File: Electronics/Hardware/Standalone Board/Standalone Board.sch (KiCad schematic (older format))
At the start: 4 parts

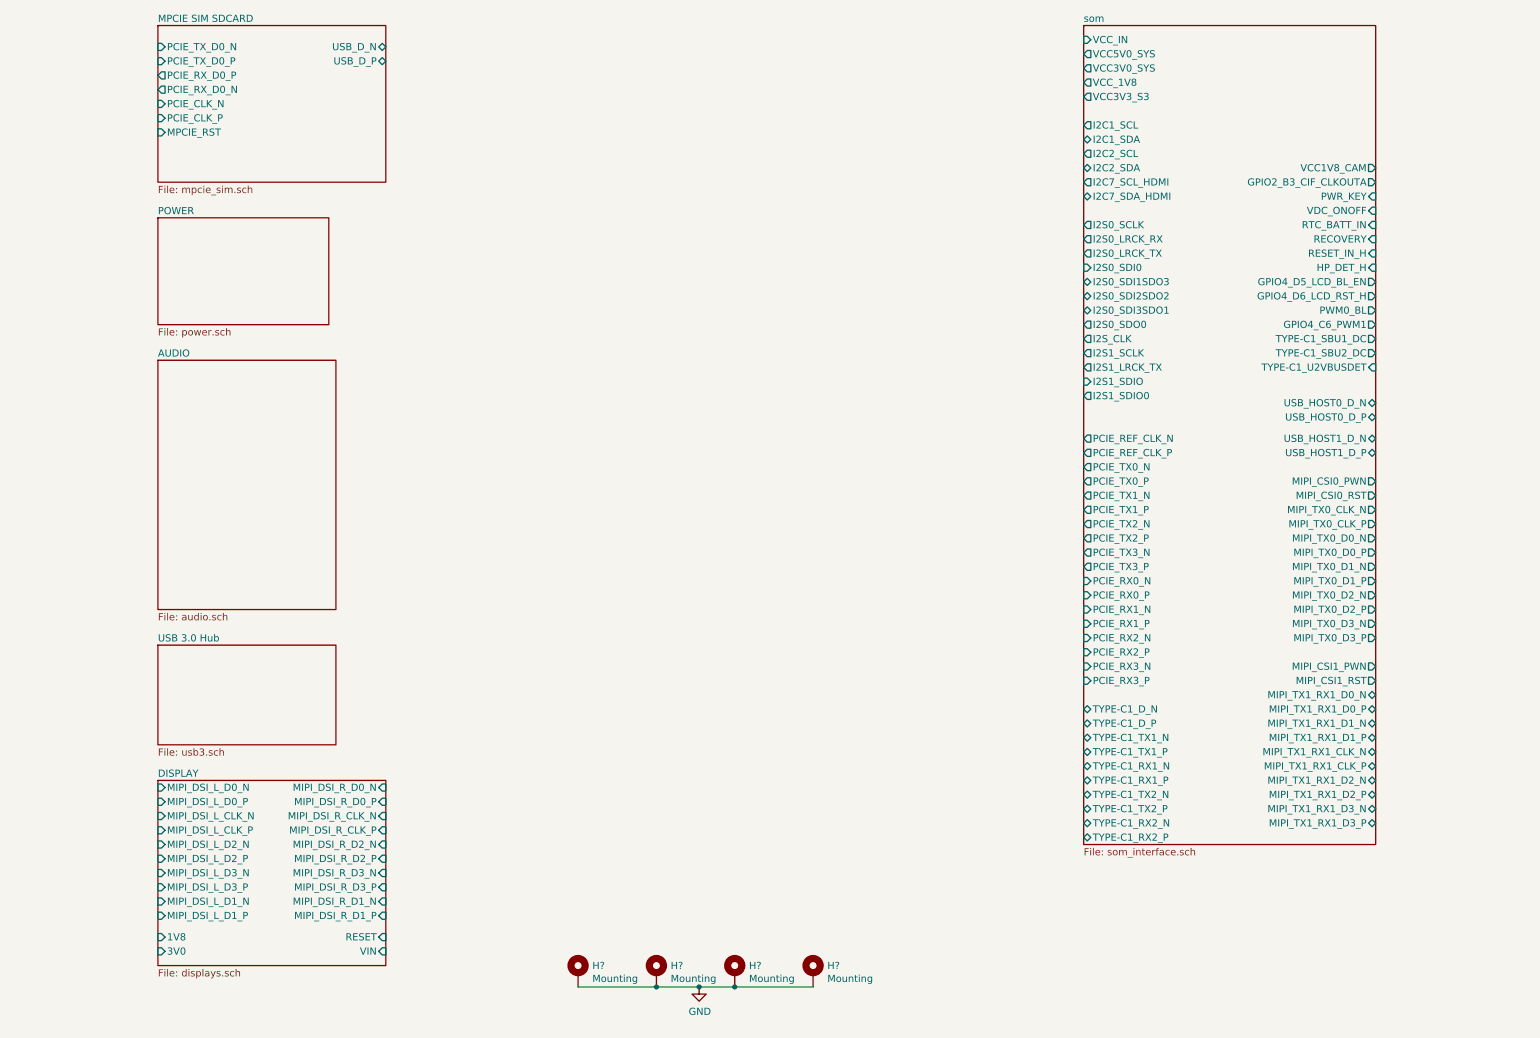
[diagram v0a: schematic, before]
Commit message: Add debug uart, gps uart, fan control and sdcard
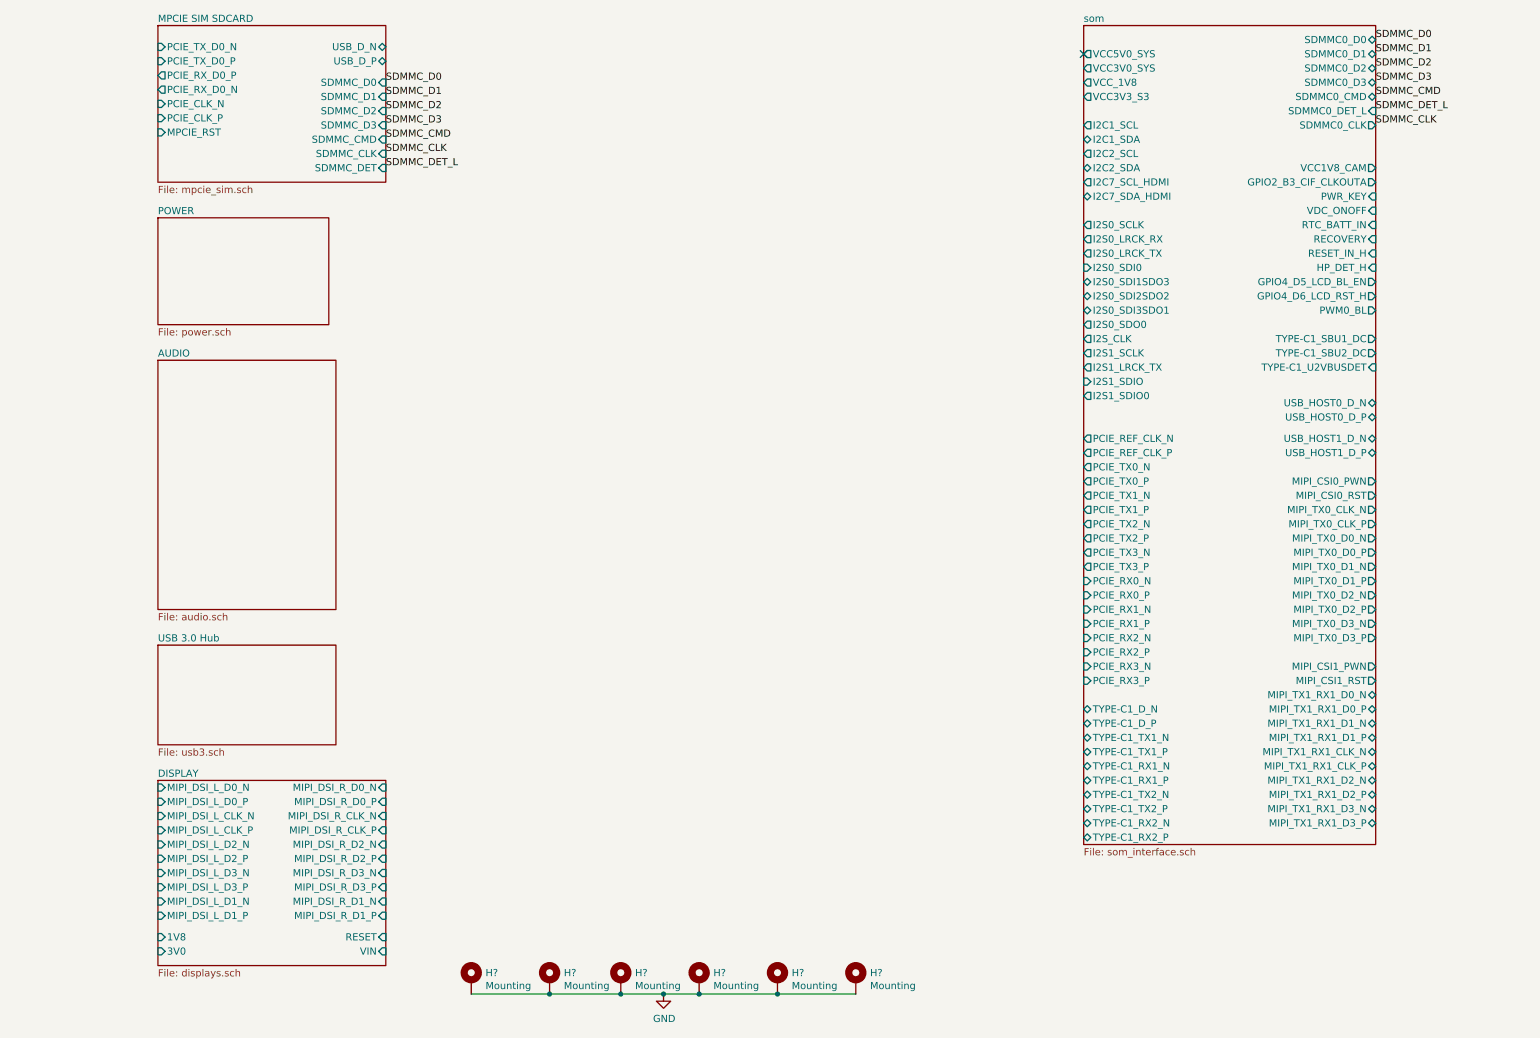
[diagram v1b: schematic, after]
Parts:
- added H? (x2): Mounting, symbol Mechanical:MountingHole_Pad
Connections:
- net GND: now also H?.1, H?.1
- no-connect marks 0 -> 1
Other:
- moved on the sheet: H?

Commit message: Add rtc, pcie + mipi dsi high level connection, usb 2.0, usb 3.0 and remove audio section
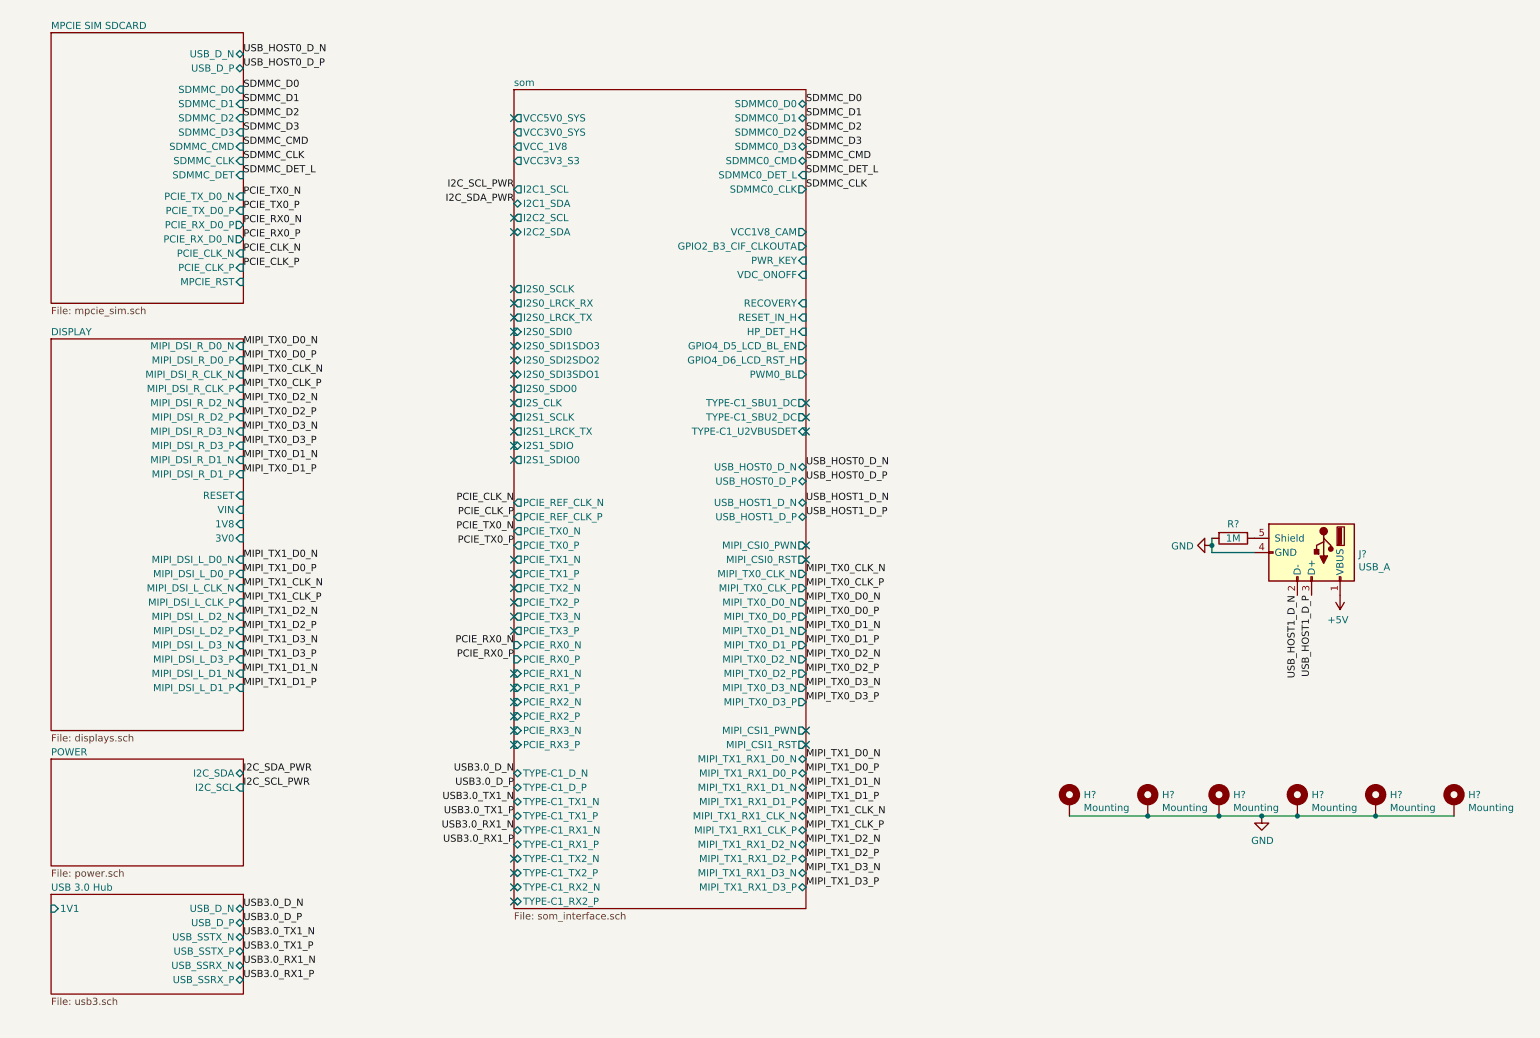
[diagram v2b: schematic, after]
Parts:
- added J?: USB_A, symbol Connector:USB_A
- added R?: 1M, symbol Device:R
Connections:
- net GND: now also J?.4 (GND), R?.2
- new net: J?.5 (Shield), R?.1
- new net +5V: J?.1 (VBUS)
- new net USB_HOST1_D_N: J?.2 (D-)
- new net USB_HOST1_D_P: J?.3 (D+)
- no-connect marks 1 -> 39
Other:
- moved on the sheet: H?

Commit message: Fix all i2c voltage, add power/reset/recovery button, Mipi dsi hig level, add 3.0/3.3/5/1.1 volt power rail
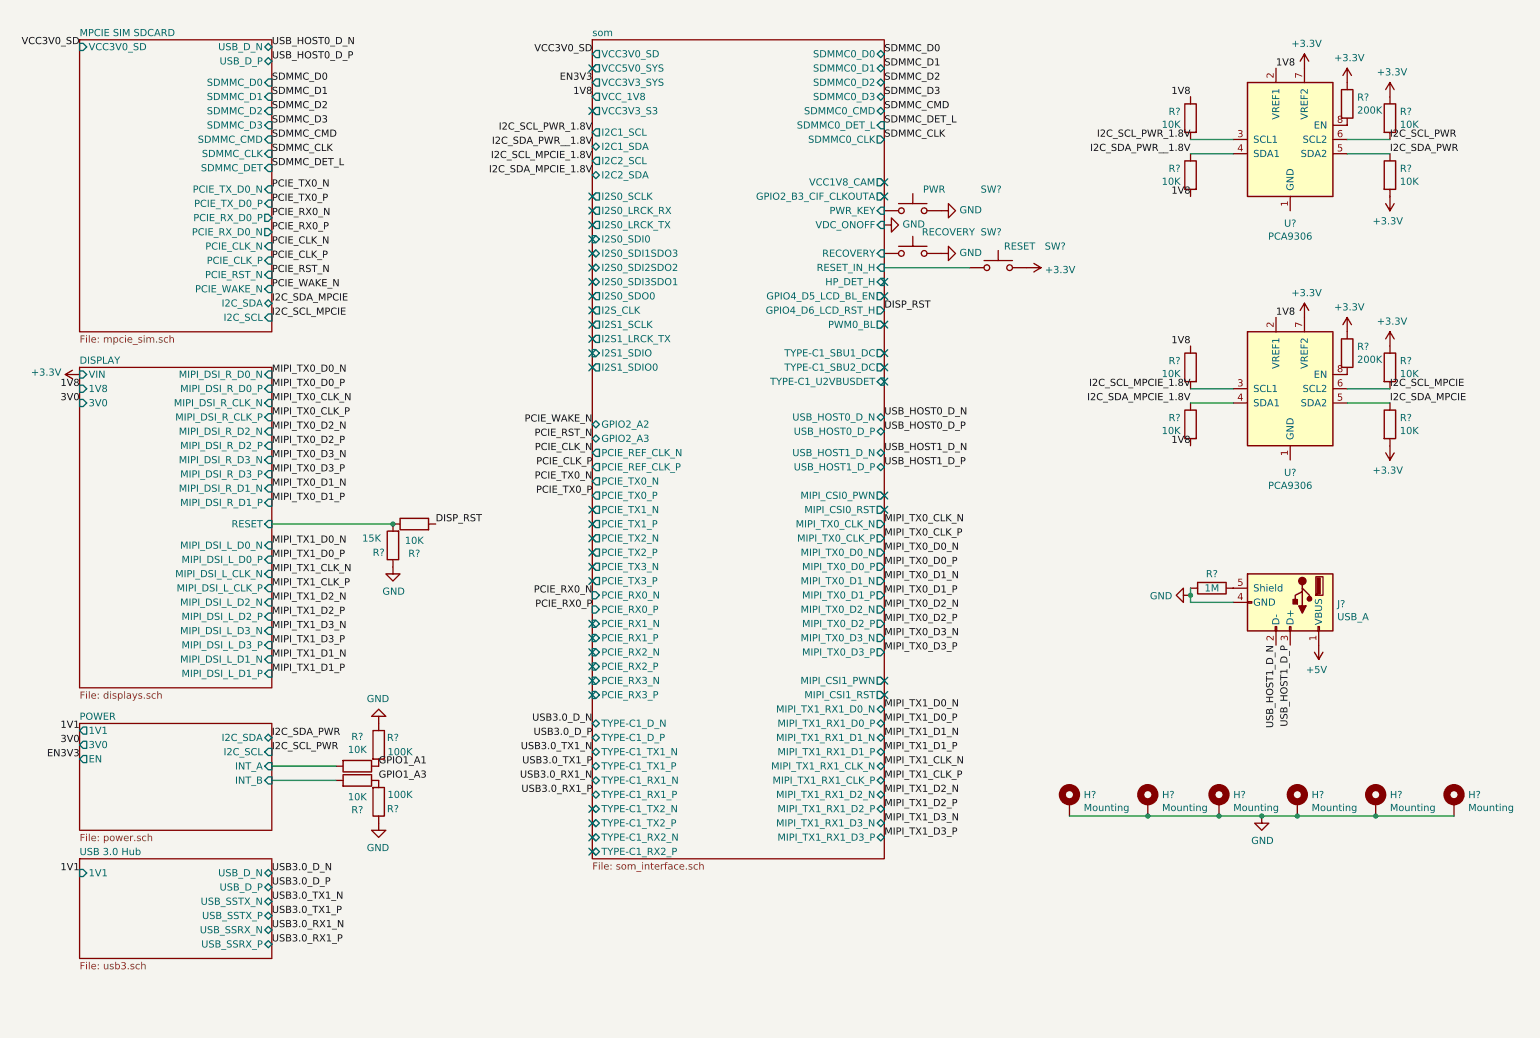
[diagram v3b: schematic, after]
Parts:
- added R? (x11): 10K, symbol Device:R
- added R? (x2): 200K, symbol Device:R
- added R? (x2): 100K, symbol Device:R
- added R?: 15K, symbol Device:R
- added SW?: PWR, symbol Switch:SW_Push
- added SW?: RECOVERY, symbol Switch:SW_Push
- added SW?: RESET, symbol Switch:SW_Push
- added U? (x2): PCA9306, symbol Interface:PCA9306
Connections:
- net DISPLAY/RESET: now also R?.1, R?.2
- net GND: now also R?.1, R?.1, R?.1, SW?.2, SW?.2
- net I2C_SCL_PWR: now also R?.2, U?.6 (SCL2)
- net I2C_SDA_PWR: now also R?.1, U?.5 (SDA2)
- net som/PWR_KEY: now also SW?.1
- net som/RECOVERY: now also SW?.1
- net som/RESET_IN_H: now also SW?.1
- new net: R?.2, U?.8 (EN) (x2)
- new net +3V3: R?.1, R?.1, R?.1, R?.1, R?.2, R?.2, SW?.2, U?.7 (VREF2), U?.7 (VREF2)
- new net 1V8: R?.1, R?.1, R?.2, R?.2, U?.2 (VREF1), U?.2 (VREF1)
- new net DISP_RST: R?.2
- new net GPIO1_A1: R?.1, R?.2
- new net GPIO1_A3: R?.1, R?.2
- new net I2C_SCL_MPCIE: R?.2, U?.6 (SCL2)
- new net I2C_SCL_MPCIE_1.8V: R?.2, U?.3 (SCL1)
- new net I2C_SCL_PWR_1.8V: R?.2, U?.3 (SCL1)
- new net I2C_SDA_MPCIE: R?.1, U?.5 (SDA2)
- new net I2C_SDA_MPCIE_1.8V: R?.1, U?.4 (SDA1)
- new net I2C_SDA_PWR__1.8V: R?.1, U?.4 (SDA1)
- new net POWER/INT_A: R?.2
- new net POWER/INT_B: R?.2
- no-connect marks 39 -> 43
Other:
- moved on the sheet: J?, R?

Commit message: Everything is routed, TODO : lenghtmatching + impedance matching + cleaning
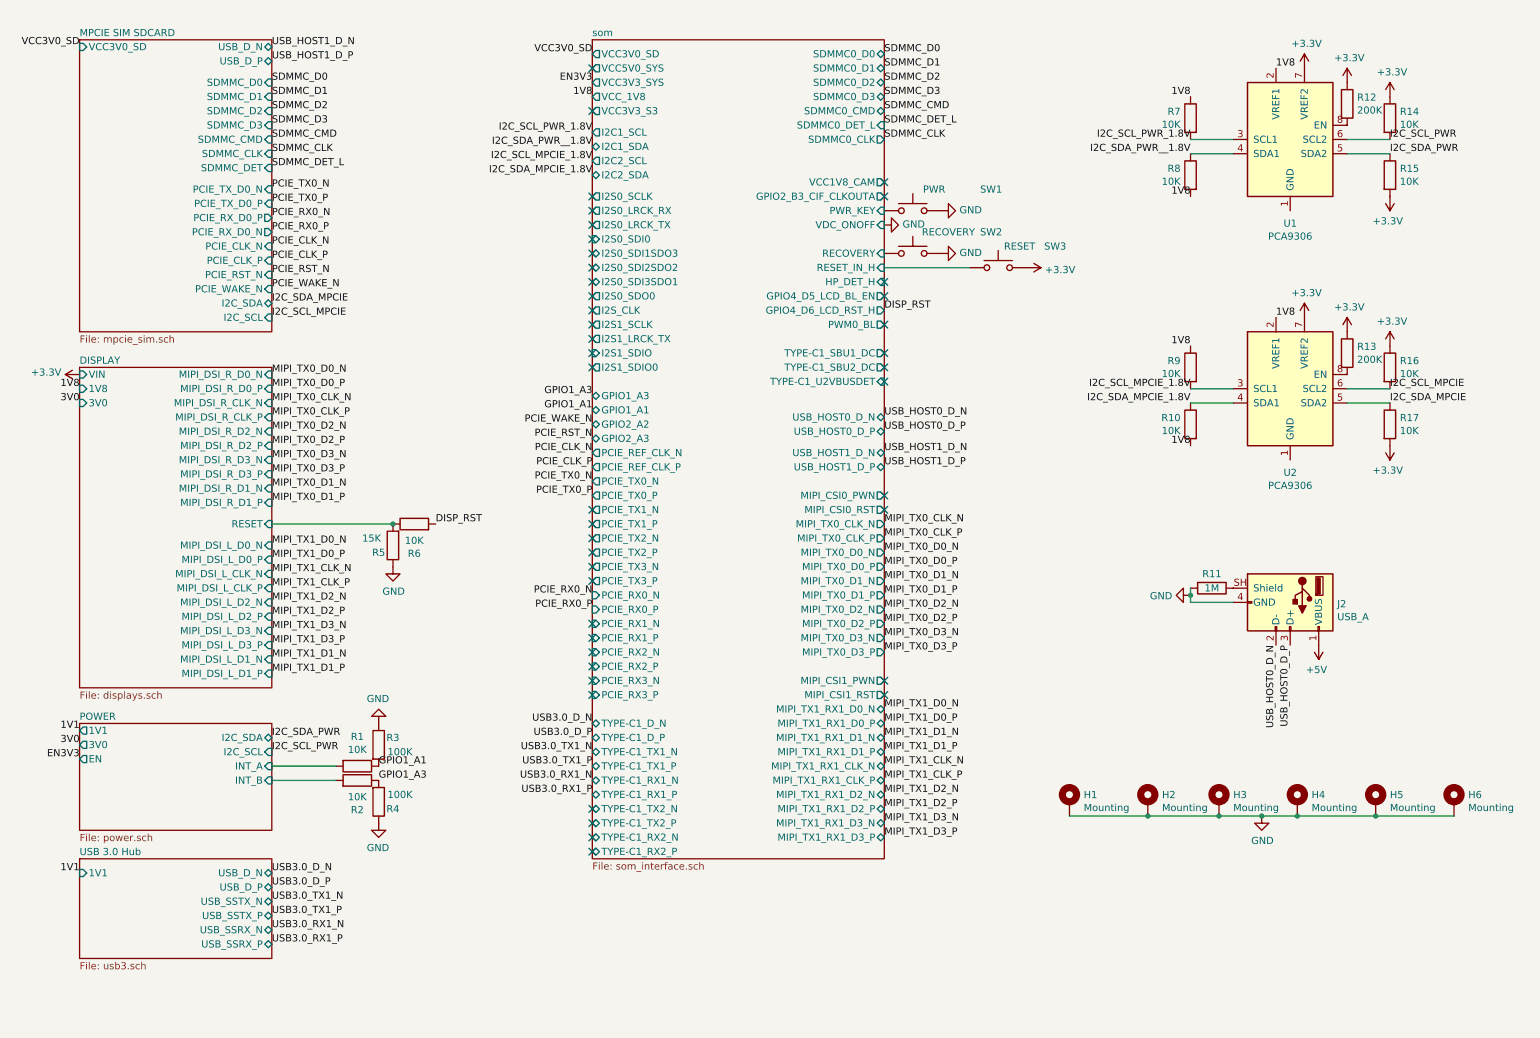
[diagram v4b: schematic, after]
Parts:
- removed J?: USB_A, symbol Connector:USB_A
- added J2: USB_A, digikey-footprints:USB_A_Female_UE27AC54100, symbol sb:USB_A
- H1, H2, H3, H4, H5, H6: renamed from H?; footprint (none) -> MountingHole:MountingHole_3.2mm_M3_Pad
- R1, R10, R11, R12, R13, R14, R15, R16, R17, R2, R3, R4, R5, R6, R7, R8, R9: renamed from R?; footprint (none) -> Resistor_SMD:R_0201_0603Metric
- SW1, SW2, SW3: renamed from SW?; footprint (none) -> Button_Switch_SMD:SW_Push_1P1T_NO_CK_KMR2
- U1, U2: renamed from U?; footprint (none) -> Package_SON:X2SON-8_1.4x1mm_P0.35mm
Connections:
- net +5V: now also J2.1 (VBUS)
- net GND: now also J2.4 (GND)
- net USB_HOST0_D_N: now also J2.2 (D-)
- net USB_HOST0_D_P: now also J2.3 (D+)
- net at R11.1: now also J2.SH (Shield)
